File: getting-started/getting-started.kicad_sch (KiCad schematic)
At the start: 0 parts

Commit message: Simple LED circuit
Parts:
- added BT1: Battery_Cell, symbol Device:Battery_Cell
- added D1: LED, symbol Device:LED
- added R1: R_US, symbol Device:R_US
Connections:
- new net GND: BT1.2 (-), D1.1 (K)
- new net VCC: BT1.1 (+), R1.1
- new net led: D1.2 (A), R1.2
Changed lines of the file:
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@@
     (rev "1")
+  )
+  (junction (at 116.84 109.22) (diameter 0) (color 0 0 0 0)
+  )
+  (junction (at 116.84 71.12) (diameter 0) (color 0 0 0 0)
+  )
+  (wire (pts (xy 116.84 109.22) (xy 97.79 109.22))
+    (stroke (width 0) (type default))
+  )
+  (wire (pts (xy 116.84 109.22) (xy 116.84 113.03))
+    (stroke (width 0) (type default))
+  )
+  (wire (pts (xy 134.62 109.22) (xy 116.84 109.22))
+    (stroke (width 0) (type default))
+  )
+  (wire (pts (xy 134.62 83.82) (xy 134.62 97.79))
+    (stroke (width 0) (type default))
+  )
+  (wire (pts (xy 116.84 71.12) (xy 134.62 71.12))
+    (stroke (width 0) (type default))
+  )
+  (wire (pts (xy 97.79 109.22) (xy 97.79 95.25))
+    (stroke (width 0) (type default))
+  )
+  (wire (pts (xy 97.79 71.12) (xy 116.84 71.12))
+    (stroke (width 0) (type default))
+  )
+  (wire (pts (xy 97.79 87.63) (xy 97.79 71.12))
+    (stroke (width 0) (type default))
+  )
+  (wire (pts (xy 116.84 68.58) (xy 116.84 71.12))
+    (stroke (width 0) (type default))
+  )
+  (wire (pts (xy 134.62 71.12) (xy 134.62 76.2))
+    (stroke (width 0) (type default))
+  )
+  (wire (pts (xy 134.62 105.41) (xy 134.62 109.22))
+    (stroke (width 0) (type default))
+  )
+  (label "led" (at 134.62 92.71 90) (fields_autoplaced)
+    (effects (font (size 1.27 1.27)) (justify left bottom))
+  )
+  (symbol (lib_id "power:VCC") (at 116.84 68.58 0) (unit 1)
+    (in_bom yes) (on_board yes) (dnp no) (fields_autoplaced)
+    (property "Reference" "#PWR02" (at 116.84 72.39 0)
+      (effects (font (size 1.27 1.27)) hide)
+    )
+    (property "Value" "VCC" (at 116.84 63.5 0)
+      (effects (font (size 1.27 1.27)))
+    )
+    (property "Footprint" "" (at 116.84 68.58 0)
+      (effects (font (size 1.27 1.27)) hide)
+    )
+    (property "Datasheet" "" (at 116.84 68.58 0)
+      (effects (font (size 1.27 1.27)) hide)
+    )
+    (pin "1")
+    (instances
+      (project "getting-started"
+        (path "/04d92c8b-6933-4953-a2b1-5fe8e7cc58f4"
+          (reference "#PWR02") (unit 1)
+        )
+      )
+    )
+  )
+  (symbol (lib_id "Device:R_US") (at 134.62 80.01 0) (unit 1)
+    (in_bom yes) (on_board yes) (dnp no) (fields_autoplaced)
+    (property "Reference" "R1" (at 137.16 78.74 0)
+      (effects (font (size 1.27 1.27)) (justify left))
+    )
+    (property "Value" "R_US" (at 137.16 81.28 0)
+      (effects (font (size 1.27 1.27)) (justify left))
+    )
+    (property "Footprint" "" (at 135.636 80.264 90)
+      (effects (font (size 1.27 1.27)) hide)
+    )
+    (property "Datasheet" "~" (at 134.62 80.01 0)
+      (effects (font (size 1.27 1.27)) hide)
+    )
+    (pin "1")
+    (pin "2")
+    (instances
+      (project "getting-started"
+        (path "/04d92c8b-6933-4953-a2b1-5fe8e7cc58f4"
+          (reference "R1") (unit 1)
+        )
+      )
+    )
+  )
+  (symbol (lib_id "Device:LED") (at 134.62 101.6 90) (unit 1)
+    (in_bom yes) (on_board yes) (dnp no) (fields_autoplaced)
+    (property "Reference" "D1" (at 138.43 101.9175 90)
+      (effects (font (size 1.27 1.27)) (justify right))
+    )
+    (property "Value" "LED" (at 138.43 104.4575 90)
+      (effects (font (size 1.27 1.27)) (justify right))
+    )
+    (property "Footprint" "" (at 134.62 101.6 0)
+      (effects (font (size 1.27 1.27)) hide)
+    )
+    (property "Datasheet" "~" (at 134.62 101.6 0)
+      (effects (font (size 1.27 1.27)) hide)
+    )
+    (pin "1")
+    (pin "2")
+    (instances
+      (project "getting-started"
+        (path "/04d92c8b-6933-4953-a2b1-5fe8e7cc58f4"
+          (reference "D1") (unit 1)
+        )
+      )
+    )
+  )
+  (symbol (lib_id "power:GND") (at 116.84 113.03 0) (unit 1)
+    (in_bom yes) (on_board yes) (dnp no) (fields_autoplaced)
+    (property "Reference" "#PWR01" (at 116.84 119.38 0)
+      (effects (font (size 1.27 1.27)) hide)
+    )
+    (property "Value" "GND" (at 116.84 118.11 0)
+      (effects (font (size 1.27 1.27)))
+    )
+    (property "Footprint" "" (at 116.84 113.03 0)
+      (effects (font (size 1.27 1.27)) hide)
+    )
+    (property "Datasheet" "" (at 116.84 113.03 0)
+      (effects (font (size 1.27 1.27)) hide)
+    )
+    (pin "1")
+    (instances
+      (project "getting-started"
+        (path "/04d92c8b-6933-4953-a2b1-5fe8e7cc58f4"
+          (reference "#PWR01") (unit 1)
+        )
+      )
+    )
+  )
+  (symbol (lib_id "Device:Battery_Cell") (at 97.79 92.71 0) (unit 1)
+    (in_bom yes) (on_board yes) (dnp no) (fields_autoplaced)
+    (property "Reference" "BT1" (at 101.6 89.5985 0)
+      (effects (font (size 1.27 1.27)) (justify left))
+    )
+    (property "Value" "Battery_Cell" (at 101.6 92.1385 0)
+      (effects (font (size 1.27 1.27)) (justify left))
+    )
+    (property "Footprint" "" (at 97.79 91.186 90)
+      (effects (font (size 1.27 1.27)) hide)
+    )
+    (property "Datasheet" "~" (at 97.79 91.186 90)
+      (effects (font (size 1.27 1.27)) hide)
+    )
+    (pin "1")
+    (pin "2")
+    (instances
+      (project "getting-started"
+        (path "/04d92c8b-6933-4953-a2b1-5fe8e7cc58f4"
+          (reference "BT1") (unit 1)
+        )
+      )
+    )
   )
   (sheet_instances

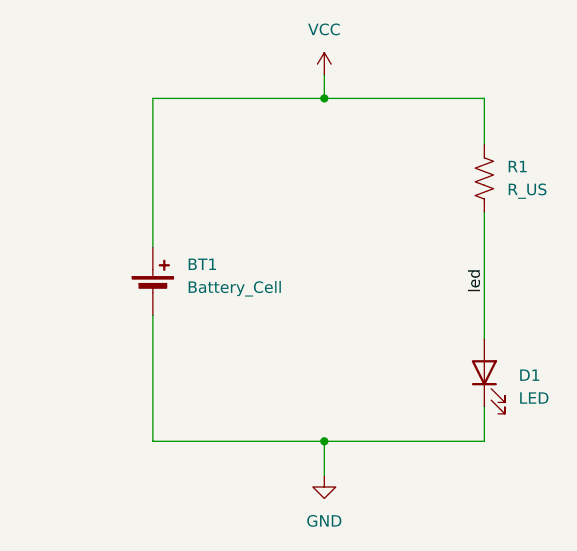
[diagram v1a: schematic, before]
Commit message: Symbol properties: 1k resistor, red led, 3V battery
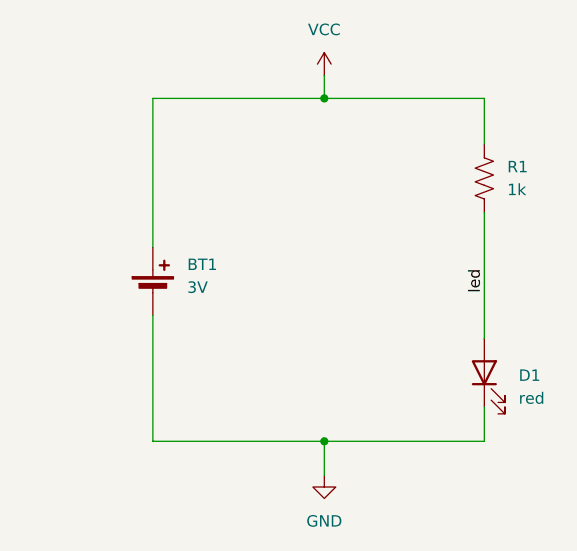
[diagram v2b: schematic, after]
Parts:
- BT1: value Battery_Cell -> 3V
- D1: value LED -> red
- R1: value R_US -> 1k
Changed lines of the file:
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@@
       (effects (font (size 1.27 1.27)) (justify left))
     )
-    (property "Value" "R_US" (at 137.16 81.28 0)
+    (property "Value" "1k" (at 137.16 81.28 0)
       (effects (font (size 1.27 1.27)) (justify left))
     )
@@
       (effects (font (size 1.27 1.27)) (justify right))
     )
-    (property "Value" "LED" (at 138.43 104.4575 90)
+    (property "Value" "red" (at 138.43 104.4575 90)
       (effects (font (size 1.27 1.27)) (justify right))
     )
@@
       (effects (font (size 1.27 1.27)) (justify left))
     )
-    (property "Value" "Battery_Cell" (at 101.6 92.1385 0)
+    (property "Value" "3V" (at 101.6 92.1385 0)
       (effects (font (size 1.27 1.27)) (justify left))
     )

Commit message: Footprint Assignment
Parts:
- BT1: footprint (none) -> Battery:BatteryHolder_Keystone_1058_1x2032
- D1: footprint (none) -> LED_THT:LED_D5.0mm
- R1: footprint (none) -> Resistor_THT:R_Axial_DIN0309_L9.0mm_D3.2mm_P12.70mm_Horizontal
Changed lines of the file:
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@@
       (effects (font (size 1.27 1.27)) (justify left))
     )
-    (property "Footprint" "" (at 135.636 80.264 90)
+    (property "Footprint" "Resistor_THT:R_Axial_DIN0309_L9.0mm_D3.2mm_P12.70mm_Horizontal" (at 135.636 80.264 90)
       (effects (font (size 1.27 1.27)) hide)
     )
@@
       (effects (font (size 1.27 1.27)) (justify right))
     )
-    (property "Footprint" "" (at 134.62 101.6 0)
+    (property "Footprint" "LED_THT:LED_D5.0mm" (at 134.62 101.6 0)
       (effects (font (size 1.27 1.27)) hide)
     )
@@
       (effects (font (size 1.27 1.27)) (justify left))
     )
-    (property "Footprint" "" (at 97.79 91.186 90)
+    (property "Footprint" "Battery:BatteryHolder_Keystone_1058_1x2032" (at 97.79 91.186 90)
       (effects (font (size 1.27 1.27)) hide)
     )

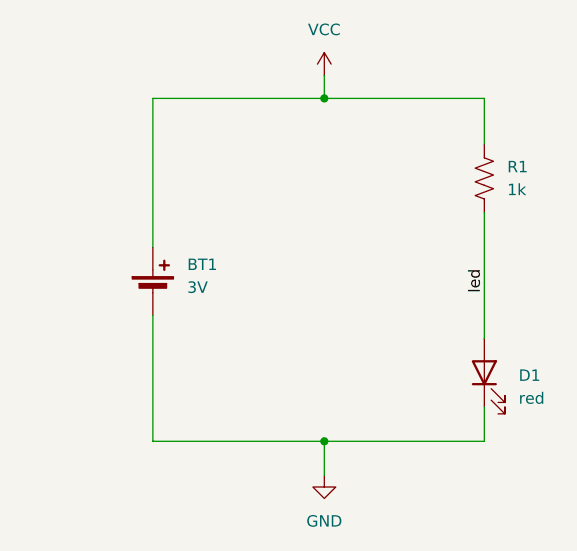
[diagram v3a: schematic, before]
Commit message: PWR_FLAG to satisfy ERC
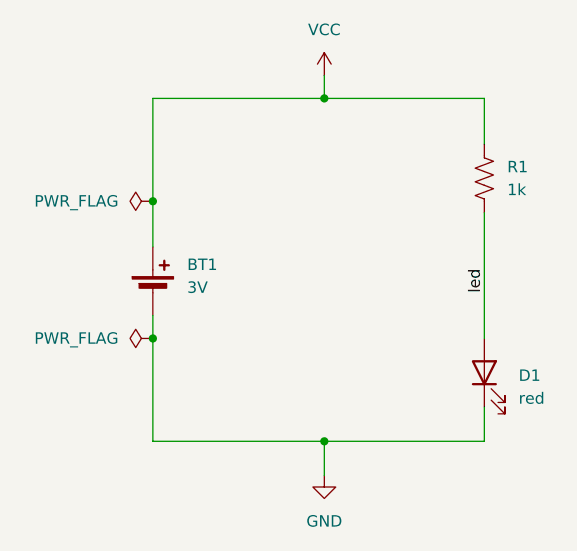
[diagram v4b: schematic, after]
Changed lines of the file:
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@@
   (junction (at 116.84 71.12) (diameter 0) (color 0 0 0 0)
+  )
+  (junction (at 97.79 82.55) (diameter 0) (color 0 0 0 0)
+  )
+  (junction (at 97.79 97.79) (diameter 0) (color 0 0 0 0)
   )
   (wire (pts (xy 116.84 109.22) (xy 97.79 109.22))
@@
     (stroke (width 0) (type default))
   )
-  (wire (pts (xy 97.79 109.22) (xy 97.79 95.25))
+  (wire (pts (xy 97.79 109.22) (xy 97.79 97.79))
     (stroke (width 0) (type default))
   )
@@
     (stroke (width 0) (type default))
   )
-  (wire (pts (xy 97.79 87.63) (xy 97.79 71.12))
+  (wire (pts (xy 97.79 87.63) (xy 97.79 82.55))
     (stroke (width 0) (type default))
   )
   (wire (pts (xy 116.84 68.58) (xy 116.84 71.12))
+    (stroke (width 0) (type default))
+  )
+  (wire (pts (xy 97.79 97.79) (xy 97.79 95.25))
     (stroke (width 0) (type default))
   )
@@
   )
   (wire (pts (xy 134.62 105.41) (xy 134.62 109.22))
+    (stroke (width 0) (type default))
+  )
+  (wire (pts (xy 97.79 82.55) (xy 97.79 71.12))
     (stroke (width 0) (type default))
   )
@@
         )
       )
+    )
+  )
+  (symbol (lib_id "power:PWR_FLAG") (at 97.79 97.79 90) (unit 1)
+    (in_bom yes) (on_board yes) (dnp no) (fields_autoplaced)
+    (property "Reference" "#FLG02" (at 95.885 97.79 0)
+      (effects (font (size 1.27 1.27)) hide)
+    )
+    (property "Value" "PWR_FLAG" (at 93.98 97.79 90)
+      (effects (font (size 1.27 1.27)) (justify left))
+    )
+    (property "Footprint" "" (at 97.79 97.79 0)
+      (effects (font (size 1.27 1.27)) hide)
+    )
+    (property "Datasheet" "~" (at 97.79 97.79 0)
+      (effects (font (size 1.27 1.27)) hide)
+    )
+    (pin "1")
+    (instances
+      (project "getting-started"
+        (path "/04d92c8b-6933-4953-a2b1-5fe8e7cc58f4"
+          (reference "#FLG02") (unit 1)
+        )
+      )
+    )
+  )
+  (symbol (lib_id "power:PWR_FLAG") (at 97.79 82.55 90) (unit 1)
+    (in_bom yes) (on_board yes) (dnp no) (fields_autoplaced)
+    (property "Reference" "#FLG01" (at 95.885 82.55 0)
+      (effects (font (size 1.27 1.27)) hide)
+    )
+    (property "Value" "PWR_FLAG" (at 93.98 82.55 90)
+      (effects (font (size 1.27 1.27)) (justify left))
+    )
+    (property "Footprint" "" (at 97.79 82.55 0)
+      (effects (font (size 1.27 1.27)) hide)
+    )
+    (property "Datasheet" "~" (at 97.79 82.55 0)
+      (effects (font (size 1.27 1.27)) hide)
+    )
+    (pin "1")
+    (instances
+      (project "getting-started"
+        (path "/04d92c8b-6933-4953-a2b1-5fe8e7cc58f4"
+          (reference "#FLG01") (unit 1)
+        )
+      )

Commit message: Add new symbol to schematic
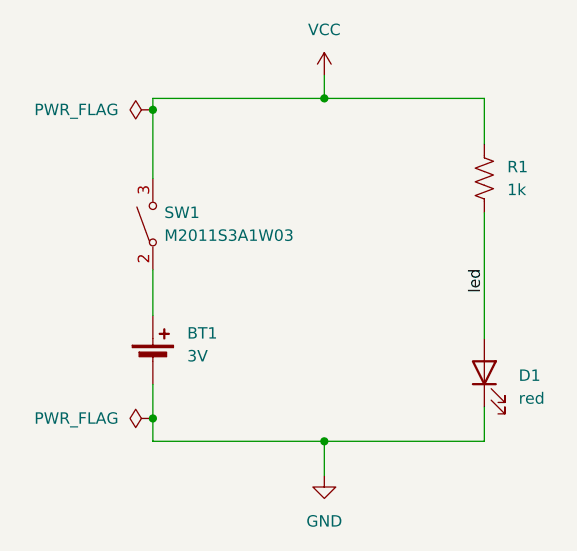
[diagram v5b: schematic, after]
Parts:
- added SW1: M2011S3A1W03, getting-started:Switch_Toggle_SPST_NKK_M2011S3A1x03, symbol getting-started:M2011S3A1W03
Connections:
- net VCC: now also SW1.3 (B); no longer BT1.1 (+)
- new net: BT1.1 (+), SW1.2 (A)
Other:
- moved on the sheet: BT1
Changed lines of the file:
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@@
   (junction (at 116.84 71.12) (diameter 0) (color 0 0 0 0)
   )
-  (junction (at 97.79 82.55) (diameter 0) (color 0 0 0 0)
-  )
-  (junction (at 97.79 97.79) (diameter 0) (color 0 0 0 0)
+  (junction (at 97.79 72.39) (diameter 0) (color 0 0 0 0)
+  )
+  (junction (at 97.79 106.68) (diameter 0) (color 0 0 0 0)
   )
   (wire (pts (xy 116.84 109.22) (xy 97.79 109.22))
@@
     (stroke (width 0) (type default))
   )
+  (wire (pts (xy 97.79 72.39) (xy 97.79 80.01))
+    (stroke (width 0) (type default))
+  )
   (wire (pts (xy 134.62 109.22) (xy 116.84 109.22))
     (stroke (width 0) (type default))
@@
     (stroke (width 0) (type default))
   )
+  (wire (pts (xy 97.79 72.39) (xy 97.79 71.12))
+    (stroke (width 0) (type default))
+  )
+  (wire (pts (xy 97.79 102.87) (xy 97.79 106.68))
+    (stroke (width 0) (type default))
+  )
   (wire (pts (xy 116.84 71.12) (xy 134.62 71.12))
     (stroke (width 0) (type default))
   )
-  (wire (pts (xy 97.79 109.22) (xy 97.79 97.79))
+  (wire (pts (xy 97.79 109.22) (xy 97.79 106.68))
     (stroke (width 0) (type default))
   )
@@
     (stroke (width 0) (type default))
   )
-  (wire (pts (xy 97.79 87.63) (xy 97.79 82.55))
-    (stroke (width 0) (type default))
-  )
   (wire (pts (xy 116.84 68.58) (xy 116.84 71.12))
     (stroke (width 0) (type default))
   )
-  (wire (pts (xy 97.79 97.79) (xy 97.79 95.25))
+  (wire (pts (xy 97.79 90.17) (xy 97.79 95.25))
     (stroke (width 0) (type default))
   )
@@
   )
   (wire (pts (xy 134.62 105.41) (xy 134.62 109.22))
-    (stroke (width 0) (type default))
-  )
-  (wire (pts (xy 97.79 82.55) (xy 97.79 71.12))
     (stroke (width 0) (type default))
   )
@@
     )
   )
-  (symbol (lib_id "power:PWR_FLAG") (at 97.79 97.79 90) (unit 1)
-    (in_bom yes) (on_board yes) (dnp no) (fields_autoplaced)
-    (property "Reference" "#FLG02" (at 95.885 97.79 0)
-      (effects (font (size 1.27 1.27)) hide)
-    )
-    (property "Value" "PWR_FLAG" (at 93.98 97.79 90)
-      (effects (font (size 1.27 1.27)) (justify left))
-    )
-    (property "Footprint" "" (at 97.79 97.79 0)
-      (effects (font (size 1.27 1.27)) hide)
-    )
-    (property "Datasheet" "~" (at 97.79 97.79 0)
+  (symbol (lib_id "getting-started:M2011S3A1W03") (at 97.79 85.09 90) (unit 1)
+    (in_bom yes) (on_board yes) (dnp no) (fields_autoplaced)
+    (property "Reference" "SW1" (at 99.06 83.82 90)
+      (effects (font (size 1.27 1.27)) (justify right))
+    )
+    (property "Value" "M2011S3A1W03" (at 99.06 86.36 90)
+      (effects (font (size 1.27 1.27)) (justify right))
+    )
+    (property "Footprint" "getting-started:Switch_Toggle_SPST_NKK_M2011S3A1x03" (at 105.41 85.09 0)
+      (effects (font (size 1.27 1.27)) hide)
+    )
+    (property "Datasheet" "" (at 97.79 85.09 0)
+      (effects (font (size 1.27 1.27)) hide)
+    )
+    (pin "2")
+    (pin "3")
+    (instances
+      (project "getting-started"
+        (path "/04d92c8b-6933-4953-a2b1-5fe8e7cc58f4"
+          (reference "SW1") (unit 1)
+        )
+      )
+    )
+  )
+  (symbol (lib_id "power:PWR_FLAG") (at 97.79 106.68 90) (unit 1)
+    (in_bom yes) (on_board yes) (dnp no)
+    (property "Reference" "#FLG02" (at 95.885 106.68 0)
+      (effects (font (size 1.27 1.27)) hide)
+    )
+    (property "Value" "PWR_FLAG" (at 93.98 106.68 90)
+      (effects (font (size 1.27 1.27)) (justify left))
+    )
+    (property "Footprint" "" (at 97.79 106.68 0)
+      (effects (font (size 1.27 1.27)) hide)
+    )
+    (property "Datasheet" "~" (at 97.79 106.68 0)
       (effects (font (size 1.27 1.27)) hide)
     )
@@
     )
   )
-  (symbol (lib_id "power:PWR_FLAG") (at 97.79 82.55 90) (unit 1)
-    (in_bom yes) (on_board yes) (dnp no) (fields_autoplaced)
-    (property "Reference" "#FLG01" (at 95.885 82.55 0)
-      (effects (font (size 1.27 1.27)) hide)
-    )
-    (property "Value" "PWR_FLAG" (at 93.98 82.55 90)
-      (effects (font (size 1.27 1.27)) (justify left))
-    )
-    (property "Footprint" "" (at 97.79 82.55 0)
-      (effects (font (size 1.27 1.27)) hide)
-    )
-    (property "Datasheet" "~" (at 97.79 82.55 0)
+  (symbol (lib_id "power:PWR_FLAG") (at 97.79 72.39 90) (unit 1)
+    (in_bom yes) (on_board yes) (dnp no) (fields_autoplaced)
+    (property "Reference" "#FLG01" (at 95.885 72.39 0)
+      (effects (font (size 1.27 1.27)) hide)
+    )
+    (property "Value" "PWR_FLAG" (at 93.98 72.39 90)
+      (effects (font (size 1.27 1.27)) (justify left))
+    )
+    (property "Footprint" "" (at 97.79 72.39 0)
+      (effects (font (size 1.27 1.27)) hide)
+    )
+    (property "Datasheet" "~" (at 97.79 72.39 0)
       (effects (font (size 1.27 1.27)) hide)
     )
@@
     )
   )
-  (symbol (lib_id "Device:Battery_Cell") (at 97.79 92.71 0) (unit 1)
-    (in_bom yes) (on_board yes) (dnp no) (fields_autoplaced)
-    (property "Reference" "BT1" (at 101.6 89.5985 0)
-      (effects (font (size 1.27 1.27)) (justify left))
-    )
-    (property "Value" "3V" (at 101.6 92.1385 0)
-      (effects (font (size 1.27 1.27)) (justify left))
-    )
-    (property "Footprint" "Battery:BatteryHolder_Keystone_1058_1x2032" (at 97.79 91.186 90)
-      (effects (font (size 1.27 1.27)) hide)
-    )
-    (property "Datasheet" "~" (at 97.79 91.186 90)
-      (effects (font (size 1.27 1.27)) hide)
-    )
+  (symbol (lib_id "Device:Battery_Cell") (at 97.79 100.33 0) (unit 1)
+    (in_bom yes) (on_board yes) (dnp no) (fields_autoplaced)
+    (property "Reference" "BT1" (at 101.6 97.2185 0)
+      (effects (font (size 1.27 1.27)) (justify left))
+    )
+    (property "Value" "3V" (at 101.6 99.7585 0)
+      (effects (font (size 1.27 1.27)) (justify left))
+    )
+    (property "Footprint" "Battery:BatteryHolder_Keystone_1058_1x2032" (at 97.79 98.806 90)
+      (effects (font (size 1.27 1.27)) hide)
+    )
+    (property "Datasheet" "~" (at 97.79 98.806 90)
+      (effects (font (size 1.27 1.27)) hide)
+    )
